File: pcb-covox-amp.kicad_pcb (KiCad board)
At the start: 2 copper layers, 80 x 56 mm, 41 parts, among them J1 DB25, P1 USB_OTG, U1 LM386, X1 MJ-2135MJ-2135, X2 MJ-2135MJ-2135

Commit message: another commit
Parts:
- D1: value Yellow LED -> Yellow
- P1: value USB_OTG -> USB
- X1: value MJ-2135MJ-2135 -> Amp
- X2: value MJ-2135MJ-2135 -> Raw
- moved X2 0.89 mm to (174.0, 106.3)
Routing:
- net Source-Audio: track 101.6 -> 102.5 mm
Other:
- board text added: "Bass"
- board text added: "Gain"
- board text added: "Vol"

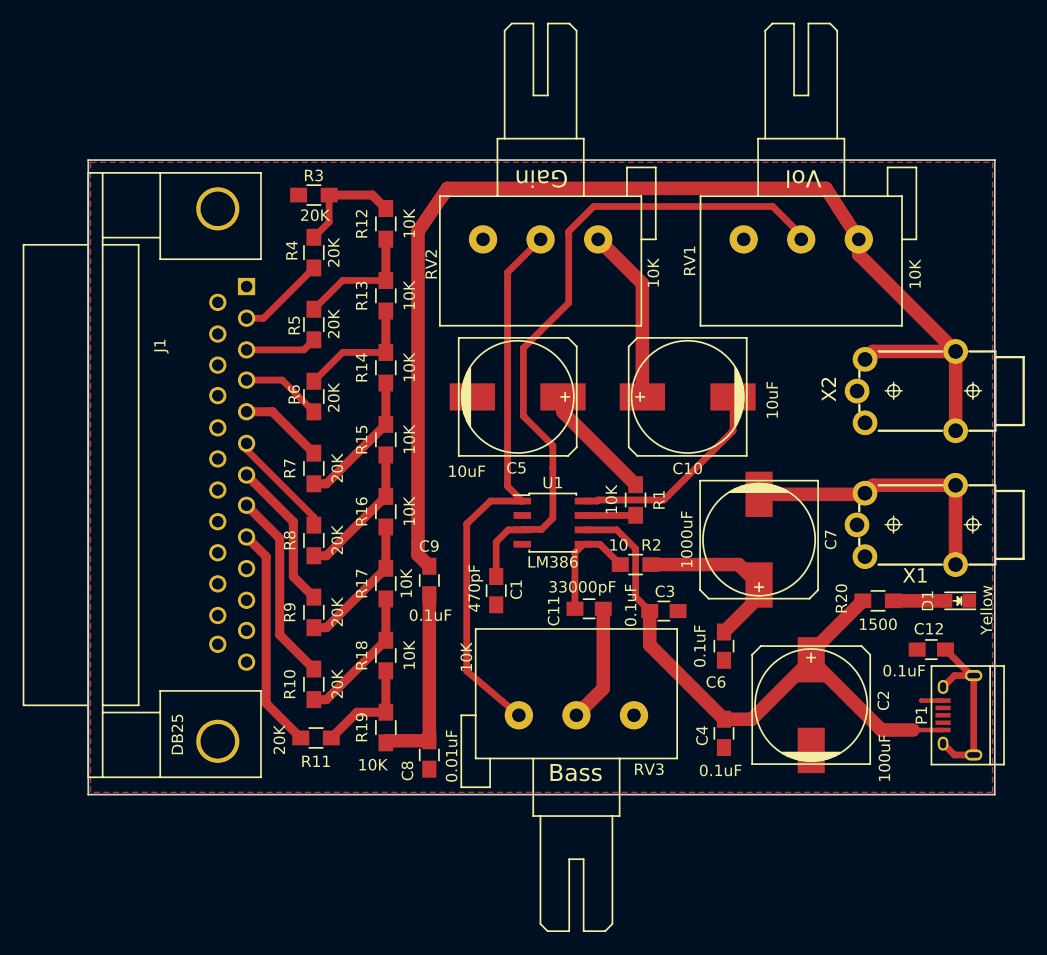
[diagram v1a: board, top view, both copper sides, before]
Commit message: curve corners
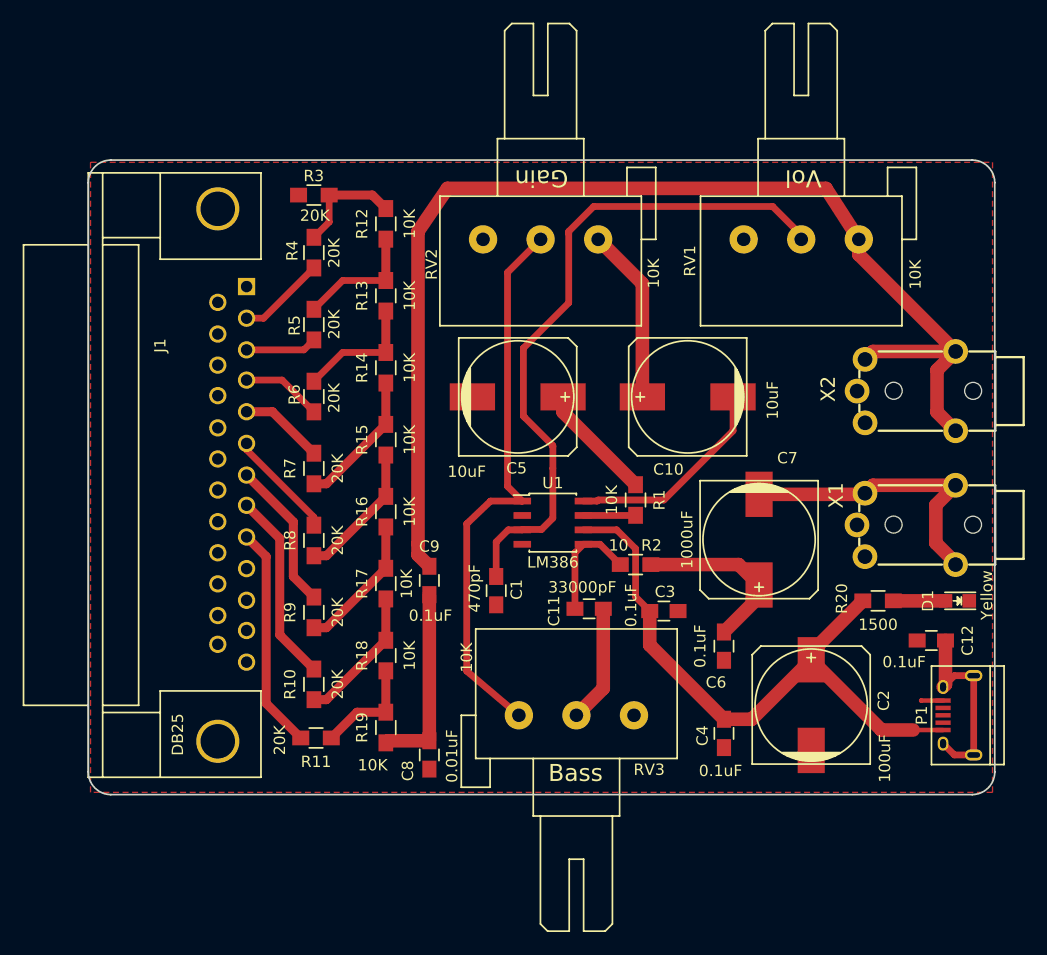
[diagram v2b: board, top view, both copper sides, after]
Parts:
- moved C12 0.80 mm to (174.4, 128.4)
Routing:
- net Amp-Audio: track 24.7 -> 26.1 mm
- net Source-Audio: track 102.5 -> 103.9 mm
- net Net-(C12-Pad2): track 16.7 -> 17.6 mm
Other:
- outline, holes or cut-outs redrawn

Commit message: silkscreen details
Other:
- board text added: "Covox Amplifier Rev 1 (July 2016) Designer: Yeo Kheng Meng"
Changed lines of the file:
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@@
     (area 99.924999 85.924999 180.075001 142.075001)
     (thickness 1.6)
-    (drawings 11)
+    (drawings 12)
     (tracks 144)
     (zones 0)
@@
     (descr "Potentiometer, Alps, RK163, single")
     (tags "Potentiometer, Alps, RK163, single")
-    (fp_text reference RV1 (at -1.9 -14.9 270) (layer F.SilkS)
+    (fp_text reference RV1 (at 4.8 -11.3 180) (layer F.SilkS)
       (effects (font (size 1 1) (thickness 0.15)))
     )
@@
     (descr "Potentiometer, Alps, RK163, single")
     (tags "Potentiometer, Alps, RK163, single")
-    (fp_text reference RV2 (at -2.2 -14.7 270) (layer F.SilkS)
-      (effects (font (size 1 1) (thickness 0.15)))
-    )
-    (fp_text value 10K (at -3 4.9 90) (layer F.SilkS)
+    (fp_text reference RV2 (at 4.7 -11.2 360) (layer F.SilkS)
+      (effects (font (size 1 1) (thickness 0.15)))
+    )
+    (fp_text value 10K (at -2.4 -14.6 270) (layer F.SilkS)
       (effects (font (size 1 1) (thickness 0.15)))
     )
@@
     (pad "" np_thru_hole circle (at 0.06 2.92 270) (size 1.5 1.5) (drill 1.5) (layers *.Cu *.Mask F.SilkS))
   )
+  (gr_text "Covox Amplifier\nRev 1 (July 2016)\nDesigner: Yeo Kheng Meng" (at 141.2 97.6) (layer F.SilkS)
+    (effects (font (size 1.5 1.5) (thickness 0.3)) (justify left))
+  )
   (gr_arc (start 178 140) (end 180 140) (angle 90) (layer Edge.Cuts) (width 0.15))
